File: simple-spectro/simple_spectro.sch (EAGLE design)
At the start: 56 parts, among them CN2 JSTPH, U1 MCP73831T-2ACI/OT, X2 16MHz, X4 MINI-USB

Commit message: starting disposition of components in simple spectro
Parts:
- removed C11: 100nF, rcl:C-EUC1206
- removed CN1: (no value), microbuilder:USB_TYPEAPCB
- removed CN2: JSTPH, microbuilder:JST_2PIN
- removed LCD: (no value), lpatiny:LCD-HEADER
- removed R6: 2K, microbuilder:RESISTOR0805
- removed RK6: 10k, resistor:R-EU_M0805
- removed SJ1: (no value), jumper:SJ
- removed SJ2: (no value), microbuilder:SOLDERJUMPER
- added C4: 100nF, dp_devices:CAPACITOR_NPOL-0805
- added CON2: JACK_DC_BARREL, lpatiny:JACK_DC_BARREL
- added CU7, CU8: 10u, rcl:C-EUC0805
- added D1, D3, D5, D6: 1N581D1206, lpatiny:1N581D1206
- added IC1: MCP1703DB, linear:MCP1703DB
- added J2: RJ12RIGHTANGLE-I2C, lpatiny:RJ12RIGHTANGLE-I2C
- added PAD1, PAD2: (no value), wirepad:SMD2
- added Q1: DMP1045U, dp_devices:TRANSISTOR_FET_TSM2301CX
- added U$11: LCD-HD447804-HOLES16X2-4-HOLES, HD44780LCD:LCD-HD447804-HOLES16X2-4-HOLES
- R3: value 1k -> 100k; device rcl:R-EU_R0805 -> microbuilder:RESISTOR0805
- RK1: value 10k -> 3.9k
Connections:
- removed net VDD1: C2.P$1, CN1.VBUS, LED1.A, U1.VDD
- new net I2C-5V: D1.A, J2.5
- new net N$15: C2.P$1, D4.C, D5.A, D6.C, LED1.A, Q1.G, R3.2, U1.VDD
- new net VCC: 32U4./RESET, CU8.1, IC1.VO
- new net VDD: CU7.1, D5.C, IC1.VI, Q1.S
- net +12V: now also D3.A, J2.1
- net +5V/1: now also D1.C, D6.A, U$11.VDD; no longer 32U4.UVCC, D4.C, LCD.2, RK1.1, RK6.2
- net A6: now also U$11.DB7; no longer LCD.14
- net D10*: now also U$11.RS; no longer LCD.4
- net D12*: now also U$11.DB6; no longer LCD.13
- net D13*: now also RK1.1
- net D6*: now also U$11.DB5; no longer LCD.12
- net D8*: now also U$11.DB4; no longer LCD.11
- net D9*: now also U$11.E; no longer LCD.6
- net GND: now also C4.2, CON2.GND, CU7.2, CU8.2, IC1.GND, J2.4, J2.6, PAD2.P, R3.1, U$11.K, U$11.R/W, U$11.VSS; no longer C11.2, CN1.GND, CN2.1, LCD.1, LCD.16, LCD.5, R3.2, R6.2, SJ1.1
- net N$11: now also U$11.A; no longer LCD.15
- net N$2: now also C4.1, U$11.VO; no longer LCD.3, R3.1
- net N$6: no longer SJ2.2
- net N$8: now also D3.C; no longer R6.1, SJ2.1
- net RESET: no longer 32U4./RESET, C11.1, RK6.1, SJ1.2
- net SCL: now also J2.2
- net SDA: now also J2.3
- net VBAT1: now also PAD1.P, Q1.D; no longer CN2.2
- net VUSB: now also 32U4.UVCC
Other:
- note added: "3.3V LDO"
- note added: "5V_12V_protect"
- note added: "Load sharing: http://blog.zakkemble.co.uk/a-lithium-battery-charger-with-load-sharing/"
- note added: "MAX 6V !"
- note added: "RGB UV"
- note added: "Solar pannel"
- note removed: "5V_protect"
- moved on the sheet: BKLD1, C1, C12, C2, C3, CU3, CU5, CU6, D4, LDPW5, LED1, LED2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

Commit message: Update simple spectro
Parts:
- removed 5V1, GND: (no value), Headerlibrary:PINHD-1X1
- removed CU5, CU6: 10uF, rcl:C-EUC1206
- removed LDO: NCP1117LPST50T3G, lpatiny:NCP1117LPST50T3G
- added L1: UV, led:LED3MM
- added Q2: DMP1045U, dp_devices:TRANSISTOR_FET_TSM2301CX
- added R6, R8: 470, microbuilder:RESISTOR0805
- added R9: 1k, rcl:R-EU_R0805
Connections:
- removed net BLUE: RL2.2
- removed net GREEN: RL3.2
- removed net RED: RL4.1
- new net N$17: D4.C, D6.C, Q2.D
- new net N$18: Q2.G, R6.1, R8.2
- new net N$19: L1.A, R9.2
- net +12V: no longer CU6.1, LDO.IN
- net +5V/1: now also R8.1; no longer 220.1, 5V1.1, CU5.1, LDO.OUT, LDO.TAB_OUT, U$11.VDD
- net A0: now also RL2.2
- net A1: now also RL4.1
- net A2: now also RL3.2
- net A3: now also R9.1
- net D11*: now also 220.1
- net GND: now also L1.C; no longer CU5.2, CU6.2, GND.1, LDO.ADJ
- net MOSI: now also U$11.VDD
- net N$15: now also Q2.S; no longer D4.C, D6.C
- net VCC: now also R6.2
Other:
- note added: "Over voltage protection * Consumption ? * Check resistance"
- note removed: "5V LDO"
- moved on the sheet: D4, D6

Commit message: Start routing
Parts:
- removed BKLD: RED, adafruit:LEDCHIP-LED0805
- removed C1: 100nF, rcl:C-EUC1206
- removed CU3, CU9: 10uF, rcl:C-EUC1206
- removed D2, D3: 1N581D1206, lpatiny:1N581D1206
- removed PAD1, PAD2: (no value), wirepad:SMD2
- removed R2: 1k, rcl:R-EU_R0805
- added CU1: 100nF, rcl:C-EUC0805
- added D7, D8: 1N581D1206, lpatiny:1N581D1206
- added RK3: 10k, resistor:R-EU_M0805
- added U$12: CONN2, lpatiny:CONN2
- added U$7: TSL237, lpatiny:TSL237
- X2: value 16MHz -> 8MHz
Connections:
- removed net +12V: D3.A, J2.1
- removed net +5V/1: 32U4.AVCC, 32U4.AVCC1, 32U4.VCC, 32U4.VCC1, C1.1, C12.2, CU3.1, D1.C, D2.C, D6.A, R13.1, R8.1, RE1.1, RE2.1, RK2.2
- removed net I2C-5V: D1.A, J2.5
- removed net N$17: D4.C, D6.C, Q2.D
- removed net N$3: BKLD.A, R2.2
- removed net N$8: D3.C
- new net EXT-VCC: D1.A
- new net HIGH-VCC: D1.C, D6.C, Q2.D, R8.1
- new net I2C+12V: D6.A, J2.1
- new net I2C+5V: D7.A, J2.5
- net A0: no longer RL2.2
- net A1: now also RL2.2; no longer RL4.1
- net A2: now also RL4.1; no longer RL3.2
- net A3: now also RL3.2; no longer R9.1
- net A4: now also R9.1
- net A5: now also R7.1
- net A6: now also U$11.RS; no longer U$11.DB7
- net D10*: now also U$11.DB7; no longer U$11.RS
- net D12*: now also U$11.E; no longer U$11.DB6
- net D13*: no longer R2.1, R7.1
- net D5*: now also U$7.OUT
- net D6*: now also U$11.DB4; no longer U$11.DB5
- net D8*: now also U$11.DB5; no longer U$11.DB4
- net D9*: now also U$11.DB6; no longer U$11.E
- net GND: now also CU1.2, U$12.1, U$7.GND; no longer BKLD.C, C1.2, CU3.2, CU9.1, PAD2.P
- net ISP+5V: now also D8.A; no longer D2.A
- net N$15: now also D4.C, D7.C, D8.C
- net RESET: now also 32U4./RESET, RK3.1
- net VBAT1: now also U$12.2; no longer PAD1.P
- net VCC: now also 32U4.AVCC, 32U4.AVCC1, 32U4.VCC, 32U4.VCC1, C12.2, CU1.1, R13.1, RE1.1, RE2.1, RK2.2, RK3.2, U$7.VDD; no longer 32U4./RESET
- net VUSB: no longer CU9.2
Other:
- note removed: "COM_LEDS"
- moved on the sheet: C10, C13, C2, D1, D4, D6, Q1

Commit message: work in progress
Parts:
- removed CON2: JACK_DC_BARREL, lpatiny:JACK_DC_BARREL
- removed D1: 1N581D1206, lpatiny:1N581D1206
- removed Q2: DMP1045U, dp_devices:TRANSISTOR_FET_TSM2301CX
- removed R6, R8: 470, microbuilder:RESISTOR0805
- added IC2: MCP1703-50, linear:MCP1703DB
- IC1: value MCP1703DB -> MCP1703-33
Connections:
- removed net EXT-VCC: D1.A
- removed net N$18: Q2.G, R6.1, R8.2
- net GND: now also IC2.GND; no longer CON2.GND
- net HIGH-VCC: now also IC2.VI; no longer D1.C, Q2.D, R8.1
- net N$15: now also IC2.VO; no longer Q2.S
- net VCC: no longer R6.2
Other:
- note removed: "Solar pannel"
- moved on the sheet: D6
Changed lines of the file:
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@@
 </variantdefs>
 <classes>
-<class number="0" name="default" width="0.2032" drill="0">
+<class number="0" name="default" width="0.4064" drill="0">
 <clearance class="0" value="0.25"/>
 </class>
-<class number="1" name="power" width="0.2032" drill="0.3048">
+<class number="1" name="power" width="0.4064" drill="0.3048">
 <clearance class="1" value="0.25"/>
 </class>
-<class number="2" name="VIN" width="0.4572" drill="0">
+<class number="2" name="VIN" width="0.4064" drill="0">
 <clearance class="2" value="0.25"/>
 </class>
-<class number="3" name="fine" width="0.254" drill="0">
+<class number="3" name="fine" width="0.4064" drill="0">
 <clearance class="3" value="0.25"/>
 </class>
-<class number="4" name="aref" width="0.3556" drill="0">
+<class number="4" name="aref" width="0.4064" drill="0">
 <clearance class="4" value="0.25"/>
 </class>
@@
 <part name="GND19" library="supply1" deviceset="GND" device=""/>
 <part name="CU8" library="rcl" deviceset="C-EU" device="C0805" value="10u"/>
-<part name="IC1" library="linear" deviceset="MCP1703" device="DB"/>
+<part name="IC1" library="linear" deviceset="MCP1703" device="DB" value="MCP1703-33"/>
 <part name="SUPPLY3" library="supply1" deviceset="VDD" device=""/>
 <part name="GND17" library="supply1" deviceset="GND" device=""/>
@@
 <part name="D4" library="lpatiny" deviceset="1N581*" device="D1206" value="1N581D1206"/>
 <part name="D6" library="lpatiny" deviceset="1N581*" device="D1206" value="1N581D1206"/>
-<part name="CON2" library="lpatiny" deviceset="JACK_DC_BARREL" device=""/>
-<part name="U$6" library="microbuilder" deviceset="GND" device=""/>
-<part name="Q2" library="dp_devices" deviceset="TRANSISTOR_FET_TSM2301CX" device="" value="DMP1045U"/>
-<part name="P+2" library="supply1" deviceset="VCC" device=""/>
-<part name="R6" library="microbuilder" deviceset="RESISTOR" device="0805" value="470"/>
-<part name="R8" library="microbuilder" deviceset="RESISTOR" device="0805" value="470"/>
 <part name="R9" library="rcl" deviceset="R-EU_" device="R0805" value="1k"/>
 <part name="GND9" library="supply1" deviceset="GND" device=""/>
@@
 <part name="D7" library="lpatiny" deviceset="1N581*" device="D1206" value="1N581D1206"/>
 <part name="D8" library="lpatiny" deviceset="1N581*" device="D1206" value="1N581D1206"/>
-<part name="D1" library="lpatiny" deviceset="1N581*" device="D1206" value="1N581D1206"/>
 <part name="CU1" library="rcl" deviceset="C-EU" device="C0805" value="100nF"/>
 <part name="RK3" library="resistor" deviceset="R-EU_" device="M0805" value="10k"/>
+<part name="IC2" library="linear" deviceset="MCP1703" device="DB" value="MCP1703-50"/>
+<part name="U$4" library="microbuilder" deviceset="GND" device=""/>
 </parts>
 <sheets>
@@
 <text x="332.74" y="190.5" size="0.508" layer="97">Load sharing:
 http://blog.zakkemble.co.uk/a-lithium-battery-charger-with-load-sharing/</text>
-<text x="205.74" y="215.9" size="1.778" layer="91">Solar pannel</text>
 <text x="86.36" y="60.96" size="5.08" layer="91">RGB UV</text>
 <text x="218.44" y="195.58" size="1.778" layer="91">Over voltage protection
@@
 <instance part="U$2" gate="G$1" x="200.66" y="162.56"/>
 <instance part="D4" gate="G$1" x="215.9" y="160.02"/>
-<instance part="D6" gate="G$1" x="215.9" y="177.8"/>
-<instance part="CON2" gate="G$1" x="213.36" y="226.06" rot="MR90"/>
-<instance part="U$6" gate="G$1" x="213.36" y="210.82"/>
-<instance part="Q2" gate="G$1" x="226.06" y="172.72" rot="MR270"/>
-<instance part="P+2" gate="VCC" x="248.92" y="193.04"/>
-<instance part="R6" gate="G$1" x="236.22" y="187.96"/>
-<instance part="R8" gate="G$1" x="220.98" y="187.96"/>
+<instance part="D6" gate="G$1" x="210.82" y="182.88"/>
 <instance part="R9" gate="G$1" x="99.06" y="17.78" rot="MR180"/>
 <instance part="GND9" gate="1" x="119.38" y="17.78" smashed="yes" rot="R90">
@@
 <instance part="D7" gate="G$1" x="215.9" y="149.86"/>
 <instance part="D8" gate="G$1" x="215.9" y="139.7"/>
-<instance part="D1" gate="G$1" x="215.9" y="170.18"/>
 <instance part="CU1" gate="G$1" x="38.1" y="35.56"/>
 <instance part="RK3" gate="G$1" x="58.42" y="185.42" rot="R180"/>
+<instance part="IC2" gate="G$1" x="226.06" y="182.88"/>
+<instance part="U$4" gate="G$1" x="226.06" y="170.18"/>
 </instances>
 <busses>
@@
 </segment>
 <segment>
-<pinref part="CON2" gate="G$1" pin="GND"/>
-<pinref part="U$6" gate="G$1" pin="GND"/>
-<wire x1="213.36" y1="215.9" x2="213.36" y2="213.36" width="0.1524" layer="91"/>
-</segment>
-<segment>
 <wire x1="114.3" y1="17.78" x2="116.84" y2="17.78" width="0.1524" layer="91"/>
 <pinref part="GND9" gate="1" pin="GND"/>
@@
 <wire x1="215.9" y1="251.46" x2="215.9" y2="248.92" width="0.1524" layer="91"/>
 <pinref part="U$8" gate="G$1" pin="GND"/>
+</segment>
+<segment>
+<pinref part="U$4" gate="G$1" pin="GND"/>
+<pinref part="IC2" gate="G$1" pin="GND"/>
+<wire x1="226.06" y1="172.72" x2="226.06" y2="175.26" width="0.1524" layer="91"/>
 </segment>
 </net>
@@
 <wire x1="38.1" y1="38.1" x2="38.1" y2="43.18" width="0.1524" layer="91"/>
 <wire x1="38.1" y1="43.18" x2="30.48" y2="43.18" width="0.1524" layer="91"/>
-</segment>
-<segment>
-<pinref part="R6" gate="G$1" pin="2"/>
-<pinref part="P+2" gate="VCC" pin="VCC"/>
-<wire x1="241.3" y1="187.96" x2="248.92" y2="187.96" width="0.1524" layer="91"/>
-<wire x1="248.92" y1="187.96" x2="248.92" y2="190.5" width="0.1524" layer="91"/>
 </segment>
 <segment>
@@
 <wire x1="342.9" y1="187.96" x2="342.9" y2="182.88" width="0.1524" layer="91"/>
 <pinref part="D5" gate="G$1" pin="A"/>
-<pinref part="Q2" gate="G$1" pin="S"/>
-<wire x1="231.14" y1="170.18" x2="233.68" y2="170.18" width="0.1524" layer="91"/>
 <pinref part="D4" gate="G$1" pin="C"/>
 <wire x1="218.44" y1="160.02" x2="233.68" y2="160.02" width="0.1524" layer="91"/>
 <wire x1="233.68" y1="160.02" x2="233.68" y2="170.18" width="0.1524" layer="91"/>
-<junction x="233.68" y="170.18"/>
 <pinref part="D7" gate="G$1" pin="C"/>
 <wire x1="218.44" y1="149.86" x2="233.68" y2="149.86" width="0.1524" layer="91"/>
@@
 <wire x1="218.44" y1="139.7" x2="233.68" y2="139.7" width="0.1524" layer="91"/>
 <wire x1="233.68" y1="139.7" x2="233.68" y2="149.86" width="0.1524" layer="91"/>
-</segment>
-</net>
-<net name="EXT-VCC" class="0">
-<segment>
-<wire x1="219.964" y1="226.06" x2="236.22" y2="226.06" width="0.1524" layer="91"/>
-<label x="226.06" y="226.06" size="1.778" layer="95"/>
-</segment>
-<segment>
-<pinref part="D1" gate="G$1" pin="A"/>
-<wire x1="213.36" y1="170.18" x2="200.66" y2="170.18" width="0.1524" layer="91"/>
-<label x="200.66" y="170.18" size="1.778" layer="95"/>
-</segment>
-</net>
-<net name="N$18" class="0">
-<segment>
-<pinref part="Q2" gate="G$1" pin="G"/>
-<wire x1="228.6" y1="175.26" x2="228.6" y2="187.96" width="0.1524" layer="91"/>
-<pinref part="R8" gate="G$1" pin="2"/>
-<wire x1="226.06" y1="187.96" x2="228.6" y2="187.96" width="0.1524" layer="91"/>
-<pinref part="R6" gate="G$1" pin="1"/>
-<wire x1="228.6" y1="187.96" x2="231.14" y2="187.96" width="0.1524" layer="91"/>
-<junction x="228.6" y="187.96"/>
+<pinref part="IC2" gate="G$1" pin="VO"/>
+<wire x1="236.22" y1="182.88" x2="236.22" y2="170.18" width="0.1524" layer="91"/>
 </segment>
 </net>
@@
 <segment>
 <pinref part="D6" gate="G$1" pin="A"/>
-<wire x1="200.66" y1="177.8" x2="213.36" y2="177.8" width="0.1524" layer="91"/>
-<label x="200.66" y="177.8" size="1.778" layer="95"/>
+<wire x1="200.66" y1="182.88" x2="208.28" y2="182.88" width="0.1524" layer="91"/>
+<label x="200.66" y="180.34" size="1.778" layer="95"/>
 </segment>
 </net>
 <net name="HIGH-VCC" class="0">
 <segment>
-<wire x1="220.98" y1="177.8" x2="220.98" y2="170.18" width="0.1524" layer="91"/>
 <pinref part="D6" gate="G$1" pin="C"/>
-<wire x1="218.44" y1="177.8" x2="220.98" y2="177.8" width="0.1524" layer="91"/>
-<pinref part="Q2" gate="G$1" pin="D"/>
-<wire x1="220.98" y1="177.8" x2="220.98" y2="182.88" width="0.1524" layer="91"/>
-<pinref part="R8" gate="G$1" pin="1"/>
-<wire x1="215.9" y1="187.96" x2="210.82" y2="187.96" width="0.1524" layer="91"/>
-<wire x1="220.98" y1="182.88" x2="210.82" y2="182.88" width="0.1524" layer="91"/>
-<wire x1="210.82" y1="182.88" x2="210.82" y2="187.96" width="0.1524" layer="91"/>
-<pinref part="D1" gate="G$1" pin="C"/>
-<wire x1="220.98" y1="170.18" x2="218.44" y2="170.18" width="0.1524" layer="91"/>
-<wire x1="210.82" y1="187.96" x2="200.66" y2="187.96" width="0.1524" layer="91"/>
-<label x="200.66" y="187.96" size="1.778" layer="95"/>
-</segment>
-</net>
+<wire x1="213.36" y1="182.88" x2="215.9" y2="182.88" width="0.1524" layer="91"/>
+<pinref part="IC2" gate="G$1" pin="VI"/>
+</segment>
+</net>

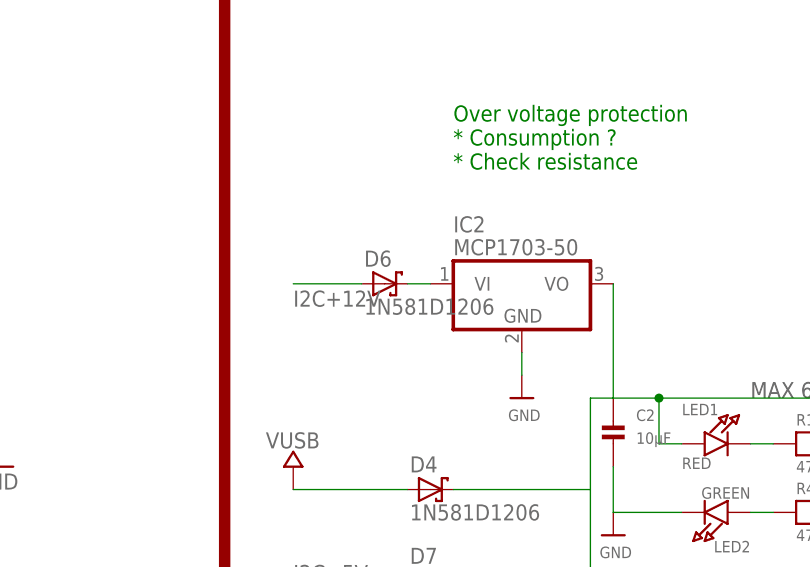
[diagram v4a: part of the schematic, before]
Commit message: removed useless D6 schottky
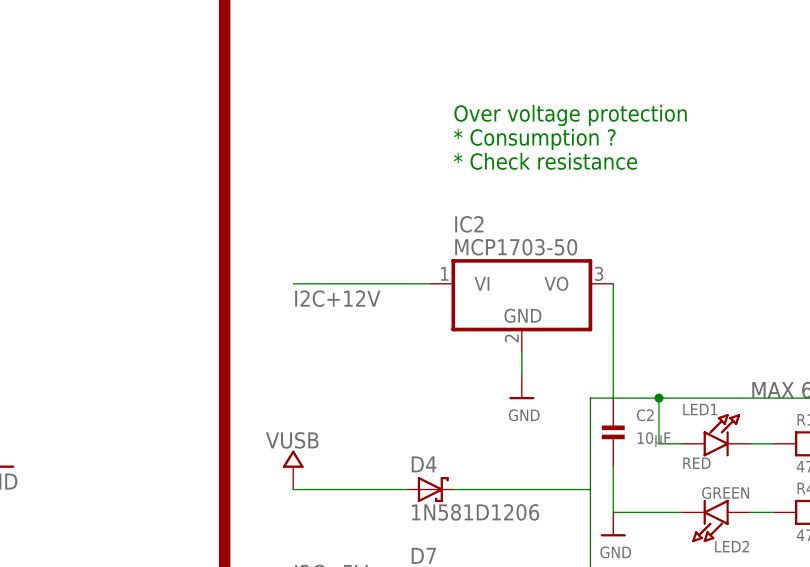
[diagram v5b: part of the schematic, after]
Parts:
- removed D6: 1N581D1206, lpatiny:1N581D1206
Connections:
- removed net HIGH-VCC: D6.C, IC2.VI
- net I2C+12V: now also IC2.VI; no longer D6.A
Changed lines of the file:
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@@
 <?xml version="1.0" encoding="utf-8"?>
 <!DOCTYPE eagle SYSTEM "eagle.dtd">
-<eagle version="7.7.0">
+<eagle version="7.5.0">
 <drawing>
 <settings>
@@
 <part name="U$2" library="MyPOW" deviceset="VUSB" device=""/>
 <part name="D4" library="lpatiny" deviceset="1N581*" device="D1206" value="1N581D1206"/>
-<part name="D6" library="lpatiny" deviceset="1N581*" device="D1206" value="1N581D1206"/>
 <part name="R9" library="rcl" deviceset="R-EU_" device="R0805" value="1k"/>
 <part name="GND9" library="supply1" deviceset="GND" device=""/>
@@
 <instance part="U$2" gate="G$1" x="200.66" y="162.56"/>
 <instance part="D4" gate="G$1" x="215.9" y="160.02"/>
-<instance part="D6" gate="G$1" x="210.82" y="182.88"/>
 <instance part="R9" gate="G$1" x="99.06" y="17.78" rot="MR180"/>
 <instance part="GND9" gate="1" x="119.38" y="17.78" smashed="yes" rot="R90">
@@
 </segment>
 <segment>
-<pinref part="D6" gate="G$1" pin="A"/>
-<wire x1="200.66" y1="182.88" x2="208.28" y2="182.88" width="0.1524" layer="91"/>
+<pinref part="IC2" gate="G$1" pin="VI"/>
+<wire x1="200.66" y1="182.88" x2="215.9" y2="182.88" width="0.1524" layer="91"/>
 <label x="200.66" y="180.34" size="1.778" layer="95"/>
 </segment>
 </net>
-<net name="HIGH-VCC" class="0">
-<segment>
-<pinref part="D6" gate="G$1" pin="C"/>
-<wire x1="213.36" y1="182.88" x2="215.9" y2="182.88" width="0.1524" layer="91"/>
-<pinref part="IC2" gate="G$1" pin="VI"/>
-</segment>
-</net>

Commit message: work in progress
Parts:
- removed RE1, RE2: 5k, rcl:R-EU_R0805
- removed RK2: 10k, resistor:R-EU_M0805
- added CON_ISP1: SPI, lpatiny:TINYISP
- added L2: UV, led:LED3MM
- added R2: 1k, rcl:R-EU_R0805
- L1: device led:LED3MM -> SparkFun:LED5MM
- RK3: value 10k -> 100k
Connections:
- new net N$8: L2.A, R2.2
- net A0: now also RL2.2
- net A1: now also RL4.1; no longer RL2.2
- net A2: now also RL3.2; no longer RL4.1
- net A3: now also R2.1; no longer RL3.2
- net D7*: no longer RK2.1
- net GND: now also CON_ISP1.GND, L2.C
- net ISP+5V: now also CON_ISP1.VCC
- net MISO: now also CON_ISP1.MISO
- net MOSI: now also CON_ISP1.MOSI
- net RESET: now also CON_ISP1.RESET
- net RX: no longer RE2.2
- net SCK: now also CON_ISP1.SCK
- net TX: no longer RE1.2
- net VCC: no longer RE1.1, RE2.1, RK2.2
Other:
- moved on the sheet: L1, R9
